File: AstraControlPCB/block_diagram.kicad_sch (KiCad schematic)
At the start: 0 parts

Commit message: Another redesign
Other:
- sheet 5V Protection ports: added none; removed VBUS
- sheet Power Connectors ports: added none; removed VBUS
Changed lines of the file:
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@@
 	)
 	(junction
-		(at 45.72 27.94)
+		(at 45.72 30.48)
 		(diameter 0)
 		(color 0 0 0 0)
@@
 	(wire
 		(pts
-			(xy 38.1 27.94) (xy 45.72 27.94)
+			(xy 38.1 30.48) (xy 45.72 30.48)
 		)
 		(stroke
@@
 		)
 	)
-	(wire
-		(pts
-			(xy 38.1 33.02) (xy 53.34 33.02)
-		)
-		(stroke
-			(width 0)
-			(type default)
-		)
-	)
 	(polyline
 		(pts
@@
 	(wire
 		(pts
-			(xy 45.72 25.4) (xy 45.72 27.94)
+			(xy 45.72 27.94) (xy 45.72 30.48)
 		)
 		(stroke
@@
 	(wire
 		(pts
-			(xy 45.72 27.94) (xy 53.34 27.94)
+			(xy 45.72 30.48) (xy 53.34 30.48)
 		)
 		(stroke
@@
 	(symbol
 		(lib_id "LiveAstra:+5V_IN")
-		(at 45.72 25.4 0)
+		(at 45.72 27.94 0)
 		(unit 1)
 		(exclude_from_sim no)
@@
 		(fields_autoplaced yes)
 		(property "Reference" "#PWR01"
-			(at 45.72 29.21 0)
+			(at 45.72 31.75 0)
 			(effects
 				(font
@@
 		)
 		(property "Value" "+5V_IN"
-			(at 45.72 20.32 0)
+			(at 45.72 22.86 0)
 			(effects
 				(font
@@
 		)
 		(property "Footprint" ""
-			(at 45.72 25.4 0)
+			(at 45.72 27.94 0)
 			(effects
 				(font
@@
 		)
 		(property "Datasheet" ""
-			(at 45.72 25.4 0)
+			(at 45.72 27.94 0)
 			(effects
 				(font
@@
 		)
 		(property "Description" "Power symbol creates a global label with name \"+5V_IN\""
-			(at 45.72 25.4 0)
+			(at 45.72 27.94 0)
 			(effects
 				(font
@@
 	)
 	(sheet
-		(at 17.78 22.86)
-		(size 20.32 66.04)
+		(at 17.78 25.4)
+		(size 20.32 63.5)
 		(fields_autoplaced yes)
 		(stroke
@@
 		)
 		(property "Sheetname" "Power Connectors"
-			(at 17.78 22.1484 0)
+			(at 17.78 24.6884 0)
 			(effects
 				(font
@@
 		)
 		(pin "5V_IN" output
-			(at 38.1 27.94 0)
-			(effects
-				(font
-					(size 1.27 1.27)
-					(thickness 0.254)
-					(bold yes)
-				)
-				(justify right)
-			)
-		)
-		(pin "VBUS" output
-			(at 38.1 33.02 0)
+			(at 38.1 30.48 0)
 			(effects
 				(font
@@
 	)
 	(sheet
-		(at 53.34 22.86)
-		(size 25.4 15.24)
+		(at 53.34 25.4)
+		(size 25.4 10.16)
 		(fields_autoplaced yes)
 		(stroke
@@
 		)
 		(property "Sheetname" "5V Protection"
-			(at 53.34 22.1484 0)
+			(at 53.34 24.6884 0)
 			(effects
 				(font
@@
 		)
 		(property "Sheetfile" "5v_protection.kicad_sch"
-			(at 53.34 38.6846 0)
+			(at 53.34 36.1446 0)
 			(effects
 				(font
@@
 		)
 		(pin "5V_IN" input
-			(at 53.34 27.94 180)
+			(at 53.34 30.48 180)
 			(effects
 				(font
@@
 			)
 		)
-		(pin "VBUS" input
-			(at 53.34 33.02 180)
-			(effects
-				(font
-					(size 1.27 1.27)
-					(thickness 0.254)
-					(bold yes)
-				)
-				(justify left)
-			)
-		)

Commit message: Reroute complete
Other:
- sheet MCU ports: added GPIO_35_TEMP_I2C_SCL, GPIO_36_TEMP_I2C_SDA, GPIO_37_FAN_PWM, GPIO_38_FAN_TACHO; removed GPIO_35_FAN_PWM, GPIO_36_FAN_TACHO, GPIO_37_TEMP_I2C_SCL, GPIO_38_TEMP_I2C_SDA

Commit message: Silkscreen
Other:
- sheet 5V GPIO Connectors ports: added GPIO_39_5V, GPIO_40_5V, GPIO_41_5V, GPIO_42_5V; removed GPIO_35_5V, GPIO_36_5V, GPIO_37_5V, GPIO_38_5V
- sheet LED PWM Connector ports: added GPIO_15_PWM_CH4, GPIO_16_PWM_CH3, GPIO_17_PWM_CH2, GPIO_18_PWM_CH1; removed PWM_CH1, PWM_CH2, PWM_CH3, PWM_CH4
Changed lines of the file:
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@@
 			)
 		)
-		(pin "GPIO_35_5V" bidirectional
+		(pin "GPIO_40_5V" bidirectional
+			(at 246.38 157.48 180)
+			(effects
+				(font
+					(size 1.27 1.27)
+					(thickness 0.254)
+					(bold yes)
+				)
+				(justify left)
+			)
+		)
+		(pin "GPIO_39_5V" bidirectional
+			(at 246.38 162.56 180)
+			(effects
+				(font
+					(size 1.27 1.27)
+					(thickness 0.254)
+					(bold yes)
+				)
+				(justify left)
+			)
+		)
+		(pin "GPIO_42_5V" bidirectional
 			(at 246.38 147.32 180)
 			(effects
@@
 			)
 		)
-		(pin "GPIO_36_5V" bidirectional
+		(pin "GPIO_41_5V" bidirectional
 			(at 246.38 152.4 180)
-			(effects
-				(font
-					(size 1.27 1.27)
-					(thickness 0.254)
-					(bold yes)
-				)
-				(justify left)
-			)
-		)
-		(pin "GPIO_37_5V" bidirectional
-			(at 246.38 157.48 180)
-			(effects
-				(font
-					(size 1.27 1.27)
-					(thickness 0.254)
-					(bold yes)
-				)
-				(justify left)
-			)
-		)
-		(pin "GPIO_38_5V" bidirectional
-			(at 246.38 162.56 180)
 			(effects
 				(font
@@
 			)
 		)
-		(pin "PWM_CH2" input
+		(pin "GPIO_17_PWM_CH2" input
 			(at 246.38 53.34 180)
 			(effects
@@
 			)
 		)
-		(pin "PWM_CH1" input
+		(pin "GPIO_18_PWM_CH1" input
 			(at 246.38 48.26 180)
 			(effects
@@
 			)
 		)
-		(pin "PWM_CH4" input
+		(pin "GPIO_15_PWM_CH4" input
 			(at 246.38 63.5 180)
 			(effects
@@
 			)
 		)
-		(pin "PWM_CH3" input
+		(pin "GPIO_16_PWM_CH3" input
 			(at 246.38 58.42 180)
 			(effects

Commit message: Update schematic titles, templates
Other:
- title: AstraControl - Root -> AstraControl - Block Diagram
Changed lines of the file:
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@@
 	(paper "A4")
 	(title_block
-		(title "AstraControl - Root")
+		(title "AstraControl - Block Diagram")
 		(date "2024-08-26")
 		(rev "A")

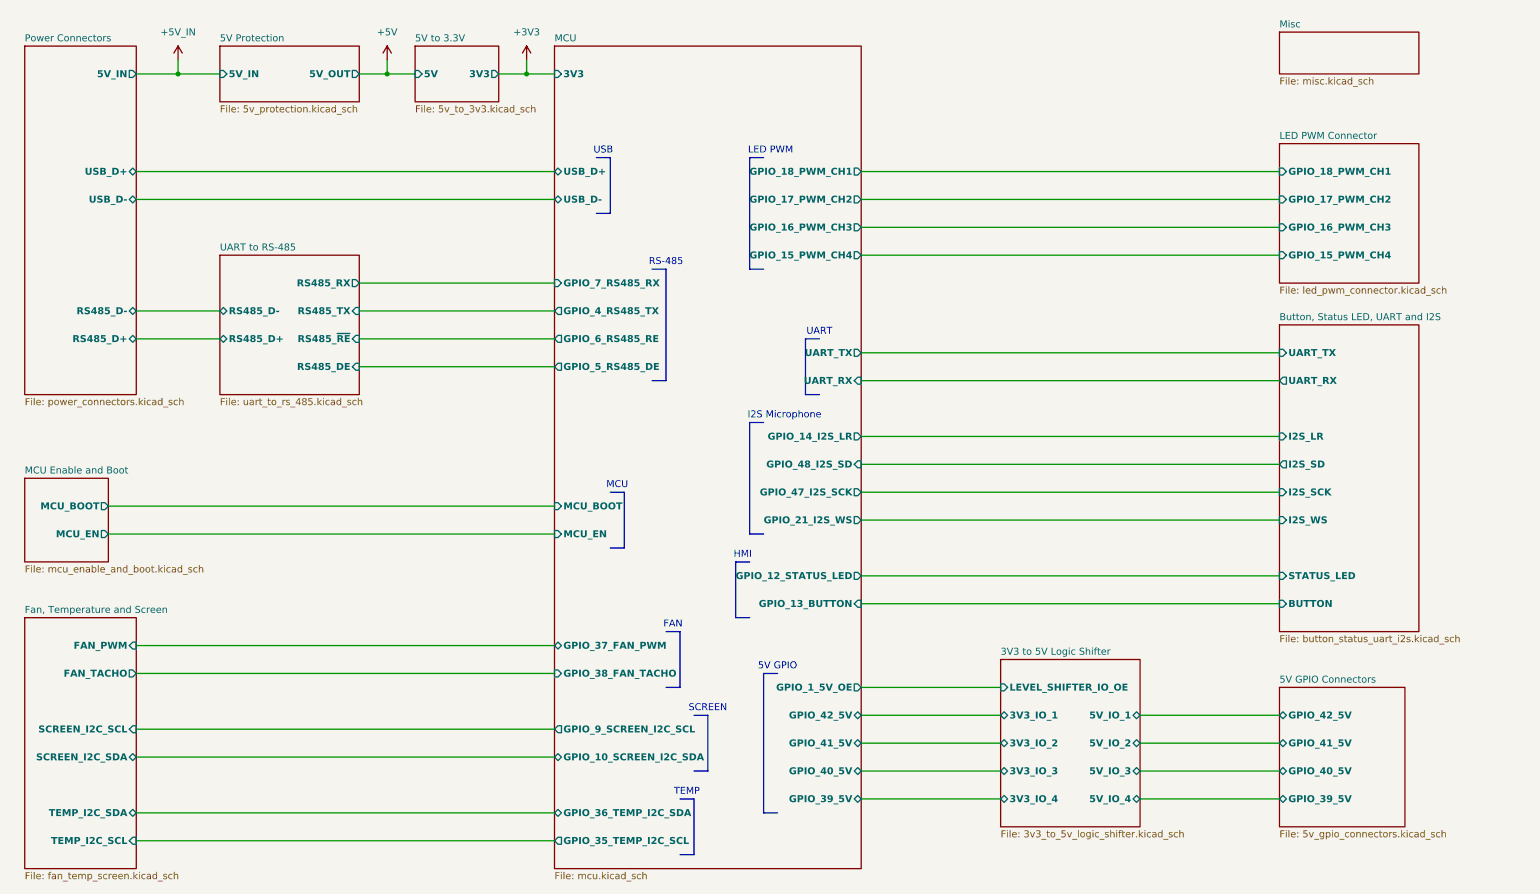
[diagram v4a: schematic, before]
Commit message: Update to new rs485 chip, use 2 bit 5v gpio
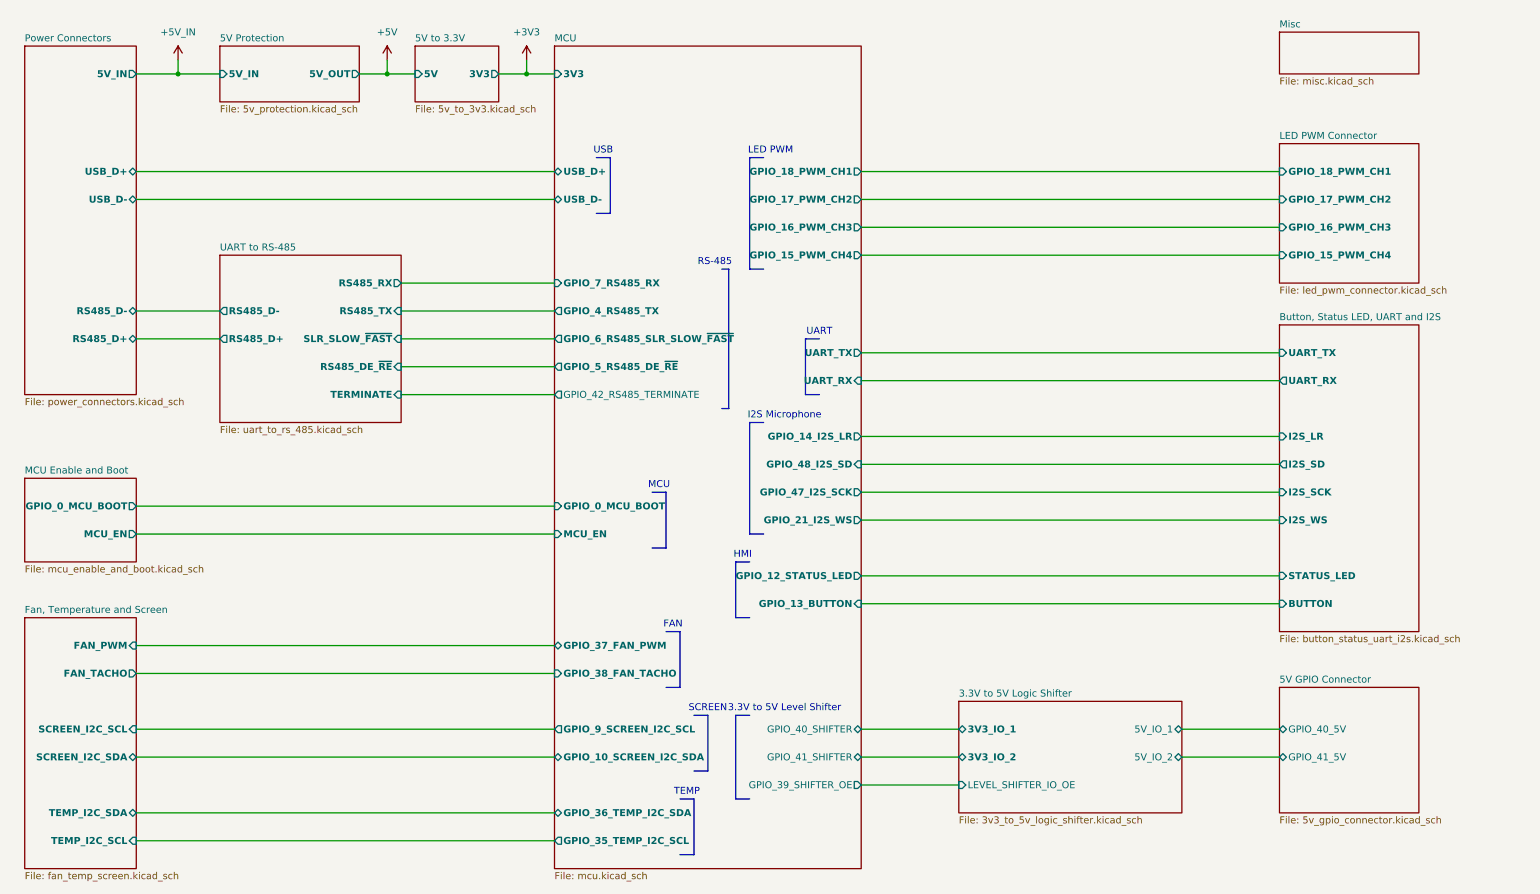
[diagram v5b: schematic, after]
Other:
- removed sheet 3V3 to 5V Logic Shifter
- removed sheet 5V GPIO Connectors
- added sheet 3.3V to 5V Logic Shifter (3v3_to_5v_logic_shifter.kicad_sch)
- added sheet 5V GPIO Connector (5v_gpio_connector.kicad_sch)
- sheet MCU ports: added GPIO_0_MCU_BOOT, GPIO_39_SHIFTER_OE, GPIO_40_SHIFTER, GPIO_41_SHIFTER, GPIO_42_RS485_TERMINATE, GPIO_5_RS485_DE_~{RE}, GPIO_6_RS485_SLR_SLOW_~{FAST}; removed GPIO_1_5V_OE, GPIO_39_5V, GPIO_40_5V, GPIO_41_5V, GPIO_42_5V, GPIO_5_RS485_DE, GPIO_6_RS485_RE, MCU_BOOT
- sheet MCU Enable and Boot ports: added GPIO_0_MCU_BOOT; removed MCU_BOOT
- sheet UART to RS-485 ports: added RS485_DE_~{RE}, SLR_SLOW_~{FAST}, TERMINATE; removed RS485_DE, RS485_~{RE}
- note added: "3.3V to 5V Level Shifter"
- note removed: "5V GPIO"

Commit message: Cleanup
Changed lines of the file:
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@@
 				(font
 					(size 1.27 1.27)
+					(thickness 0.254)
+					(bold yes)
 				)
 				(justify right)
@@
 				(font
 					(size 1.27 1.27)
+					(thickness 0.254)
+					(bold yes)
 				)
 				(justify right)
@@
 				(font
 					(size 1.27 1.27)
+					(thickness 0.254)
+					(bold yes)
 				)
 				(justify left)
@@
 				(font
 					(size 1.27 1.27)
+					(thickness 0.254)
+					(bold yes)
 				)
 				(justify right)
@@
 				(font
 					(size 1.27 1.27)
+					(thickness 0.254)
+					(bold yes)
 				)
 				(justify left)
@@
 				(font
 					(size 1.27 1.27)
-				)
-				(justify left)
-			)
-		)
-		(instances
-			(project "AstraControl"
-				(path "/9a751838-dce8-4d69-8a02-736625ac74e7/0db21d8e-3390-4d67-877f-0e5d98e37848"
-					(page "16")
+					(thickness 0.254)
+					(bold yes)
+				)
+				(justify left)
+			)
+		)
+		(instances
+			(project "AstraControl"
+				(path "/9a751838-dce8-4d69-8a02-736625ac74e7/0db21d8e-3390-4d67-877f-0e5d98e37848"
+					(page "14")
 				)
 			)
@@
 			(project "AstraControl"
 				(path "/9a751838-dce8-4d69-8a02-736625ac74e7/0db21d8e-3390-4d67-877f-0e5d98e37848"
-					(page "13")
+					(page "11")
 				)
 			)
@@
 				(font
 					(size 1.27 1.27)
+					(thickness 0.254)
+					(bold yes)
 				)
 				(justify right)
@@
 				(font
 					(size 1.27 1.27)
+					(thickness 0.254)
+					(bold yes)
 				)
 				(justify right)
@@
 				(font
 					(size 1.27 1.27)
-				)
-				(justify left)
-			)
-		)
-		(instances
-			(project "AstraControl"
-				(path "/9a751838-dce8-4d69-8a02-736625ac74e7/0db21d8e-3390-4d67-877f-0e5d98e37848"
-					(page "15")
+					(thickness 0.254)
+					(bold yes)
+				)
+				(justify left)
+			)
+		)
+		(instances
+			(project "AstraControl"
+				(path "/9a751838-dce8-4d69-8a02-736625ac74e7/0db21d8e-3390-4d67-877f-0e5d98e37848"
+					(page "13")
 				)
 			)
@@
 			(project "AstraControl"
 				(path "/9a751838-dce8-4d69-8a02-736625ac74e7/0db21d8e-3390-4d67-877f-0e5d98e37848"
-					(page "14")
-				)
-			)
+					(page "12")
+				)
+			)

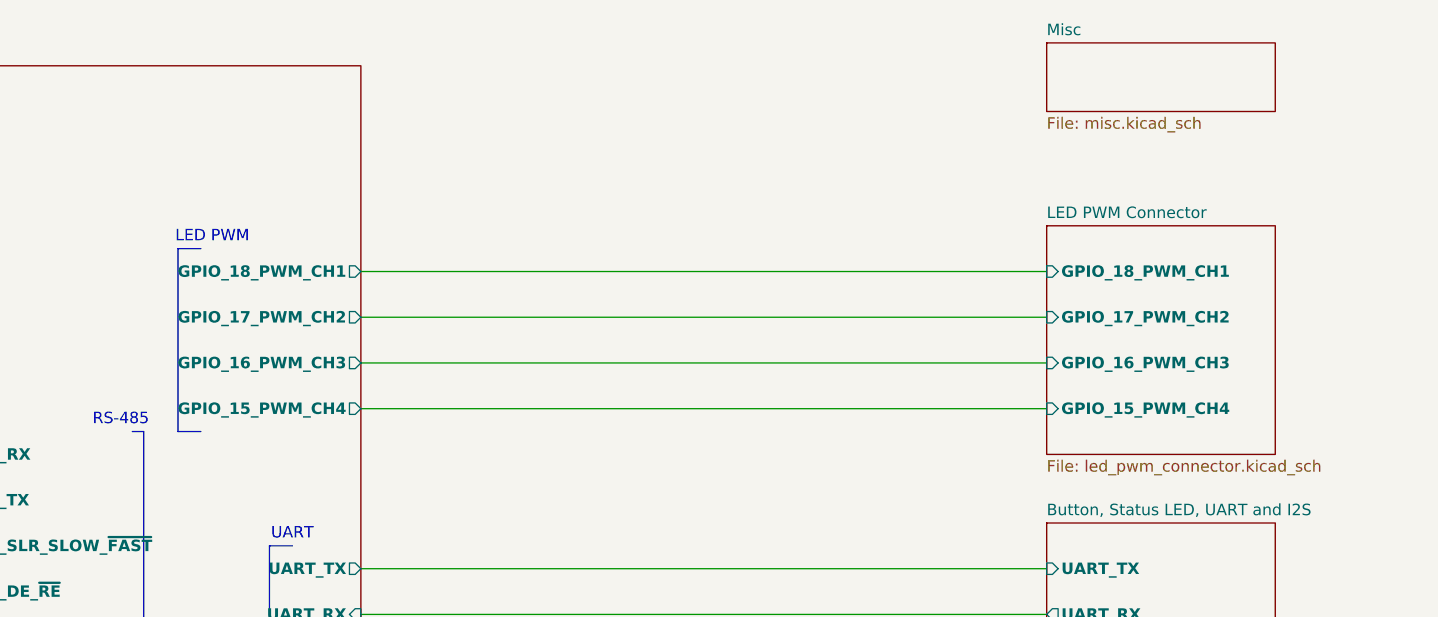
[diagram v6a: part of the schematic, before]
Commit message: Fix silkscreen on copper, add GPIO 8 to connector
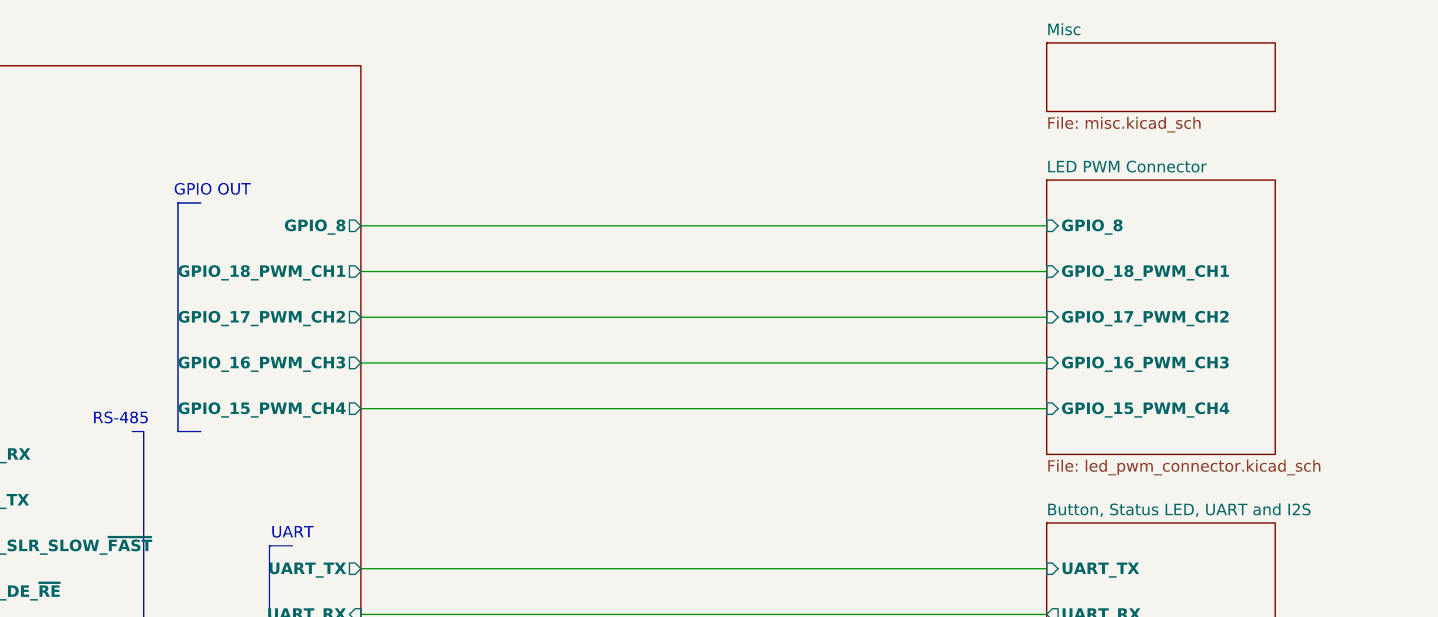
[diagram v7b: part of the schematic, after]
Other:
- sheet LED PWM Connector ports: added GPIO_8; removed none
- sheet MCU ports: added GPIO_8; removed none
- note added: "GPIO OUT"
- note removed: "LED PWM"
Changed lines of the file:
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@@
 	(polyline
 		(pts
-			(xy 149.86 45.72) (xy 152.4 45.72)
+			(xy 149.86 40.64) (xy 152.4 40.64)
 		)
 		(stroke
@@
 		)
 	)
+	(wire
+		(pts
+			(xy 170.18 43.18) (xy 246.38 43.18)
+		)
+		(stroke
+			(width 0)
+			(type default)
+		)
+	)
 	(polyline
 		(pts
@@
 	(polyline
 		(pts
-			(xy 149.86 45.72) (xy 149.86 66.04)
+			(xy 149.86 40.64) (xy 149.86 66.04)
 		)
 		(stroke
@@
 		)
 	)
-	(text "LED PWM"
+	(text "GPIO OUT"
 		(exclude_from_sim no)
-		(at 153.67 44.45 0)
+		(at 153.67 39.37 0)
 		(effects
 			(font
@@
 			)
 		)
+		(pin "GPIO_8" output
+			(at 170.18 43.18 0)
+			(effects
+				(font
+					(size 1.27 1.27)
+					(thickness 0.254)
+					(bold yes)
+				)
+				(justify right)
+			)
+		)
 		(instances
 			(project "AstraControl"
@@
 	)
 	(sheet
-		(at 246.38 43.18)
-		(size 25.4 25.4)
+		(at 246.38 38.1)
+		(size 25.4 30.48)
 		(fields_autoplaced yes)
 		(stroke
@@
 		)
 		(property "Sheetname" "LED PWM Connector"
-			(at 246.38 42.4684 0)
+			(at 246.38 37.3884 0)
 			(effects
 				(font
@@
 			(effects
 				(font
+					(size 1.27 1.27)
+					(thickness 0.254)
+					(bold yes)
+				)
+				(justify left)
+			)
+		)
+		(pin "GPIO_8" input
+			(at 246.38 43.18 180)
+			(effects
+				(font

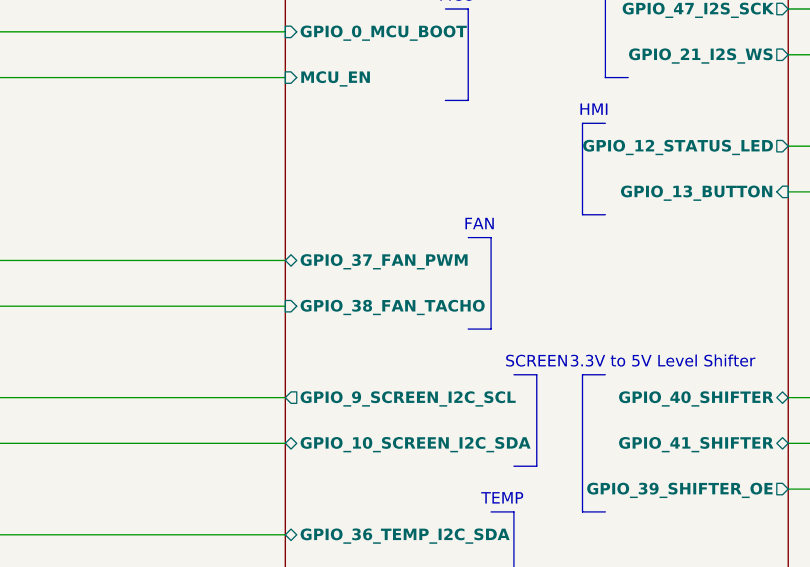
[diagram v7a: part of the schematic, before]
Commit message: Update fan to rpi style pinout, minor cosmetic fixes
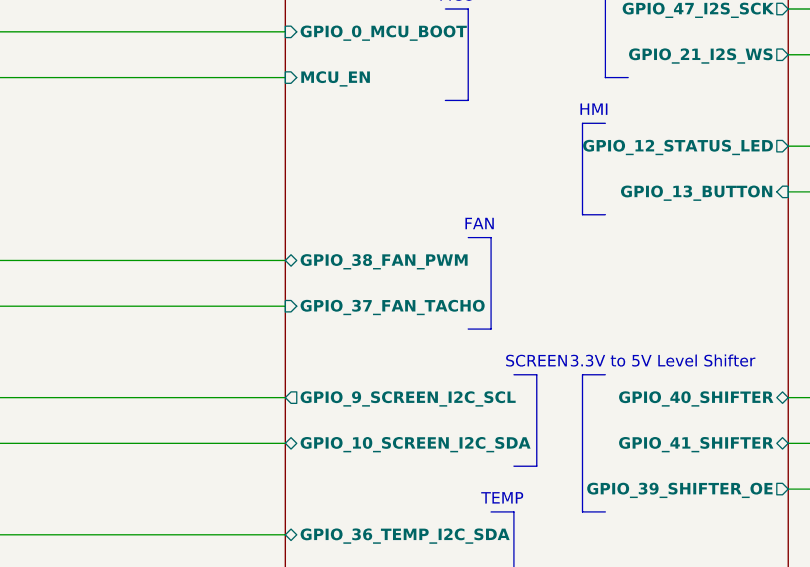
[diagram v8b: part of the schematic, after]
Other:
- sheet MCU ports: added GPIO_37_FAN_TACHO, GPIO_38_FAN_PWM; removed GPIO_37_FAN_PWM, GPIO_38_FAN_TACHO
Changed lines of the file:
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@@
-			)
-		)
-		(pin "GPIO_38_FAN_TACHO" input
-			(at 114.3 139.7 180)
-			(effects
-				(font
-					(size 1.27 1.27)
-					(thickness 0.254)
-					(bold yes)
-				)
-				(justify left)
 			)
 		)
 		(pin "GPIO_36_TEMP_I2C_SDA" bidirectional
 			(at 114.3 165.1 180)
-			(effects
-				(font
-					(size 1.27 1.27)
-					(thickness 0.254)
-					(bold yes)
-				)
-				(justify left)
-			)
-		)
-		(pin "GPIO_37_FAN_PWM" bidirectional
-			(at 114.3 134.62 180)
 			(effects
 				(font
@@
 			)
 		)
+		(pin "GPIO_37_FAN_TACHO" input
+			(at 114.3 139.7 180)
+			(effects
+				(font
+					(size 1.27 1.27)
+					(thickness 0.254)
+					(bold yes)
+				)
+				(justify left)
+			)
+		)
+		(pin "GPIO_38_FAN_PWM" bidirectional
+			(at 114.3 134.62 180)
+			(effects
+				(font
+					(size 1.27 1.27)
+					(thickness 0.254)
+					(bold yes)
+				)
+				(justify left)
+			)
+		)
